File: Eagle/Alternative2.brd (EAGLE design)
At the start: 67 x 53 mm, 19 parts, among them IC2 PCA82C251, Q1 16MHz

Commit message: update1 hw review
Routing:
- net PD0: track 0.00 -> 35.3 mm
- net PB2: track 20.3 -> 0.00 mm, vias 1 -> 0
- net PC5: track 23.4 -> 18.5 mm
- net N$6: track 11.4 -> 15.1 mm, vias 1 -> 0
- net PC4: track 19.0 -> 17.2 mm
- net +5V: track 115.0 -> 116.5 mm
- net N$7: vias 1 -> 0
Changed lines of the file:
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@@
 <contactref element="CT12" pad="1"/>
 <contactref element="U$1" pad="8"/>
-<wire x1="30.1625" y1="8.5725" x2="30.1625" y2="12.065" width="0.4064" layer="1"/>
-<wire x1="30.1625" y1="12.065" x2="29.21" y2="13.0175" width="0.4064" layer="1"/>
-<wire x1="29.21" y1="13.0175" x2="26.6725" y2="13.0175" width="0.4064" layer="1"/>
 <wire x1="39.6875" y1="3.8125" x2="44.935" y2="3.8125" width="0.4064" layer="1"/>
 <wire x1="44.935" y1="3.8125" x2="45.0725" y2="3.95" width="0.4064" layer="1"/>
@@
 <contactref element="U$3" pad="18"/>
 <wire x1="28.0162" y1="8.255" x2="29.845" y2="8.255" width="0.4064" layer="1"/>
-<wire x1="29.845" y1="8.255" x2="30.1625" y2="8.5725" width="0.4064" layer="1"/>
 <wire x1="39.6875" y1="3.8125" x2="34.2875" y2="3.8125" width="0.4064" layer="1"/>
 <wire x1="34.2875" y1="3.8125" x2="29.845" y2="8.255" width="0.4064" layer="1"/>
@@
 <wire x1="19.685" y1="19.05" x2="19.685" y2="21.5425" width="0.4064" layer="1"/>
 <wire x1="19.685" y1="21.5425" x2="19.7325" y2="21.59" width="0.4064" layer="1"/>
-<wire x1="16.825" y1="13.0175" x2="23.81" y2="13.0175" width="0.4064" layer="1"/>
 <wire x1="37.8968" y1="19.3675" x2="39.6875" y2="19.3675" width="0.4064" layer="1"/>
 <wire x1="39.6875" y1="19.3675" x2="40.3225" y2="18.7325" width="0.4064" layer="1"/>
 <wire x1="40.3225" y1="18.7325" x2="40.3225" y2="14.335" width="0.4064" layer="1"/>
-<wire x1="40.3225" y1="14.335" x2="27.035" y2="14.335" width="0.4064" layer="1"/>
-<wire x1="27.035" y1="14.335" x2="26.67" y2="13.97" width="0.4064" layer="1"/>
-<wire x1="26.6725" y1="13.0175" x2="26.67" y2="13.97" width="0" layer="19" extent="1-1"/>
-<wire x1="23.81" y1="13.0175" x2="26.6725" y2="13.0175" width="0" layer="19" extent="1-1"/>
+<wire x1="40.3225" y1="14.335" x2="35.925" y2="14.335" width="0.4064" layer="1"/>
+<wire x1="35.925" y1="14.335" x2="34.6075" y2="13.0175" width="0.4064" layer="1"/>
+<wire x1="34.6075" y1="13.0175" x2="29.845" y2="8.255" width="0.4064" layer="1"/>
+<wire x1="17.4625" y1="13.0175" x2="34.6075" y2="13.0175" width="0.4064" layer="1"/>
+<wire x1="16.825" y1="13.0175" x2="17.4625" y2="13.0175" width="0" layer="19" extent="1-1"/>
 </signal>
 <signal name="PB3">
@@
 <contactref element="SV2" pad="4"/>
 <contactref element="U$1" pad="1"/>
-<wire x1="22.7838" y1="8.255" x2="22.7838" y2="10.0863" width="0.4064" layer="1"/>
-<wire x1="22.7838" y1="8.255" x2="12.065" y2="8.255" width="0.4064" layer="1"/>
-<wire x1="12.065" y1="8.255" x2="10.795" y2="9.525" width="0.4064" layer="1"/>
-<wire x1="10.795" y1="9.525" x2="7.9375" y2="9.525" width="0.4064" layer="1"/>
-<wire x1="7.9375" y1="9.525" x2="6.6675" y2="8.255" width="0.4064" layer="1"/>
+<wire x1="22.7838" y1="8.255" x2="11.1125" y2="8.255" width="0.4064" layer="1"/>
+<wire x1="11.1125" y1="8.255" x2="9.8425" y2="6.985" width="0.4064" layer="1"/>
+<wire x1="9.8425" y1="6.985" x2="7.9375" y2="6.985" width="0.4064" layer="1"/>
+<wire x1="7.9375" y1="6.985" x2="6.6675" y2="8.255" width="0.4064" layer="1"/>
 </signal>
 <signal name="PC5">
 <contactref element="SV2" pad="2"/>
 <contactref element="U$1" pad="2"/>
-<wire x1="6.6675" y1="5.715" x2="7.9375" y2="6.985" width="0.4064" layer="1"/>
-<wire x1="7.9375" y1="6.985" x2="22.7838" y2="6.985" width="0.4064" layer="1"/>
-<wire x1="26.67" y1="11.1125" x2="25.0825" y2="9.525" width="0.4064" layer="1"/>
-<wire x1="25.0825" y1="9.525" x2="25.0825" y2="7.62" width="0.4064" layer="1"/>
-<wire x1="25.0825" y1="7.62" x2="24.4475" y2="6.985" width="0.4064" layer="1"/>
-<wire x1="24.4475" y1="6.985" x2="22.7838" y2="6.985" width="0.4064" layer="1"/>
+<wire x1="22.7838" y1="6.985" x2="13.0175" y2="6.985" width="0.4064" layer="1"/>
+<wire x1="13.0175" y1="6.985" x2="9.525" y2="3.4925" width="0.4064" layer="1"/>
+<wire x1="9.525" y1="3.4925" x2="8.89" y2="3.4925" width="0.4064" layer="1"/>
+<wire x1="8.89" y1="3.4925" x2="6.6675" y2="5.715" width="0.4064" layer="1"/>
 </signal>
 <signal name="N$4">
@@
 <contactref element="IC2" pad="4"/>
 <contactref element="U$3" pad="2"/>
-<wire x1="37.8968" y1="18.0975" x2="35.56" y2="18.0975" width="0.4064" layer="1"/>
-<via x="35.56" y="18.0975" extent="1-16" drill="0.6" shape="square"/>
-<wire x1="35.56" y1="18.0975" x2="35.56" y2="22.86" width="0.4064" layer="16"/>
-<wire x1="35.56" y1="22.86" x2="34.29" y2="24.13" width="0.4064" layer="16"/>
-<wire x1="34.29" y1="24.13" x2="31.75" y2="24.13" width="0.4064" layer="16"/>
+<wire x1="37.8968" y1="18.0975" x2="31.4325" y2="18.0975" width="0.4064" layer="1"/>
+<wire x1="31.4325" y1="18.0975" x2="29.5275" y2="20.0025" width="0.4064" layer="1"/>
+<wire x1="29.5275" y1="20.0025" x2="29.5275" y2="23.495" width="0.4064" layer="1"/>
+<wire x1="29.5275" y1="23.495" x2="30.1625" y2="24.13" width="0.4064" layer="1"/>
+<wire x1="30.1625" y1="24.13" x2="31.75" y2="24.13" width="0.4064" layer="1"/>
 </signal>
 <signal name="N$7">
 <contactref element="IC2" pad="1"/>
 <contactref element="U$3" pad="1"/>
-<wire x1="37.8968" y1="21.9075" x2="34.29" y2="21.9075" width="0.4064" layer="1"/>
-<via x="34.29" y="21.9075" extent="1-16" drill="0.6" shape="square"/>
-<wire x1="34.29" y1="21.9075" x2="32.0675" y2="21.9075" width="0.4064" layer="16"/>
-<wire x1="32.0675" y1="21.9075" x2="31.75" y2="21.59" width="0.4064" layer="16"/>
+<wire x1="37.8968" y1="21.9075" x2="35.2425" y2="21.9075" width="0.4064" layer="1"/>
+<wire x1="35.2425" y1="21.9075" x2="34.925" y2="21.59" width="0.4064" layer="1"/>
+<wire x1="34.925" y1="21.59" x2="31.75" y2="21.59" width="0.4064" layer="1"/>
 </signal>
 <signal name="N$8">
@@
 <contactref element="SV2" pad="3"/>
 <contactref element="U$3" pad="16"/>
-<wire x1="9.2075" y1="8.255" x2="24.13" y2="26.67" width="0" layer="19" extent="1-1"/>
+<wire x1="24.13" y1="26.67" x2="12.3825" y2="26.67" width="0.4064" layer="1"/>
+<wire x1="12.3825" y1="26.67" x2="10.4775" y2="24.765" width="0.4064" layer="1"/>
+<wire x1="10.4775" y1="24.765" x2="8.5725" y2="24.765" width="0.4064" layer="1"/>
+<wire x1="8.5725" y1="24.765" x2="7.9375" y2="24.13" width="0.4064" layer="1"/>
+<wire x1="7.9375" y1="24.13" x2="7.9375" y2="18.0975" width="0.4064" layer="1"/>
+<wire x1="7.9375" y1="18.0975" x2="8.89" y2="17.145" width="0.4064" layer="1"/>
+<wire x1="8.89" y1="17.145" x2="9.8425" y2="17.145" width="0.4064" layer="1"/>
+<wire x1="9.8425" y1="17.145" x2="10.4775" y2="16.51" width="0.4064" layer="1"/>
+<wire x1="10.4775" y1="16.51" x2="10.4775" y2="9.525" width="0.4064" layer="1"/>
+<wire x1="10.4775" y1="9.525" x2="9.2075" y2="8.255" width="0.4064" layer="1"/>
 </signal>
 <signal name="PD1">
@@
 <signal name="PB2">
 <contactref element="SV2" pad="26"/>
-<wire x1="6.6675" y1="36.195" x2="7.9375" y2="37.465" width="0.4064" layer="1"/>
-<wire x1="7.9375" y1="37.465" x2="14.605" y2="37.465" width="0.4064" layer="1"/>
-<via x="14.605" y="37.465" extent="1-16" drill="0.6" shape="square"/>
-<wire x1="14.605" y1="37.465" x2="14.605" y2="29.21" width="0.4064" layer="16"/>
-<wire x1="14.605" y1="29.21" x2="17.145" y2="26.67" width="0.4064" layer="16"/>
 </signal>
 <signal name="N$16">

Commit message: Update2
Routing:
- net +5V: vias 1 -> 0
- net N$4: vias 1 -> 0
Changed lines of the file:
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@@
 <wire x1="27.94" y1="36.83" x2="26.67" y2="38.1" width="0.4064" layer="16"/>
 <wire x1="26.67" y1="38.1" x2="19.3675" y2="38.1" width="0.4064" layer="16"/>
-<wire x1="24.13" y1="21.59" x2="21.9075" y2="21.59" width="0.4064" layer="16"/>
-<via x="21.9075" y="21.59" extent="1-16" drill="0.6" shape="square"/>
-<wire x1="21.9075" y1="21.59" x2="19.7325" y2="21.59" width="0.4064" layer="1"/>
 <wire x1="16.825" y1="13.0175" x2="16.825" y2="16.19" width="0.4064" layer="1"/>
 <wire x1="16.825" y1="16.19" x2="19.685" y2="19.05" width="0.4064" layer="1"/>
@@
 <wire x1="34.6075" y1="13.0175" x2="29.845" y2="8.255" width="0.4064" layer="1"/>
 <wire x1="17.4625" y1="13.0175" x2="34.6075" y2="13.0175" width="0.4064" layer="1"/>
+<wire x1="19.7325" y1="21.59" x2="24.13" y2="21.59" width="0.4064" layer="1"/>
 <wire x1="16.825" y1="13.0175" x2="17.4625" y2="13.0175" width="0" layer="19" extent="1-1"/>
 </signal>
@@
 <wire x1="19.685" y1="25.0825" x2="19.685" y2="24.1775" width="0.4064" layer="1"/>
 <wire x1="19.685" y1="24.1775" x2="19.7325" y2="24.13" width="0.4064" layer="1"/>
-<wire x1="24.13" y1="24.13" x2="21.9075" y2="24.13" width="0.4064" layer="16"/>
-<via x="21.9075" y="24.13" extent="1-16" drill="0.6" shape="square"/>
-<wire x1="21.9075" y1="24.13" x2="19.7325" y2="24.13" width="0.4064" layer="1"/>
+<wire x1="19.7325" y1="24.13" x2="24.13" y2="24.13" width="0.4064" layer="1"/>
 </signal>
 <signal name="N$5">

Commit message: Update3
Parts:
- moved R10 2.54 mm to (47.9, 17.5)
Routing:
- net N$9: track 4.13 -> 6.67 mm
- net PD6: track 23.4 -> 22.4 mm
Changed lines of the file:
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@@
 <attribute name="MF" value="" x="37.1475" y="38.1" size="1.778" layer="27" rot="R90" display="off"/>
 </element>
-<element name="R10" library="rcl" package="R0805" value="120" x="47.9425" y="20.0025" smashed="yes" rot="R270">
-<attribute name="NAME" x="49.2125" y="17.145" size="1.27" layer="25" rot="R3"/>
-<attribute name="VALUE" x="49.2125" y="15.5575" size="1.27" layer="27"/>
+<element name="R10" library="rcl" package="R0805" value="120" x="47.9425" y="17.4625" smashed="yes" rot="R270">
+<attribute name="NAME" x="49.2125" y="14.605" size="1.27" layer="25" rot="R3"/>
+<attribute name="VALUE" x="49.2125" y="13.0175" size="1.27" layer="27"/>
 </element>
 <element name="R8" library="rcl" package="R0805" value="10k" x="15.875" y="13.0175" smashed="yes">
@@
 <wire x1="44.935" y1="3.8125" x2="45.0725" y2="3.95" width="0.4064" layer="1"/>
 <wire x1="9.2075" y1="20.955" x2="10.4775" y2="20.955" width="0.4064" layer="1"/>
-<wire x1="10.4775" y1="20.955" x2="11.43" y2="20.0025" width="0.4064" layer="1"/>
-<wire x1="11.43" y1="20.0025" x2="11.43" y2="12.065" width="0.4064" layer="1"/>
-<wire x1="11.43" y1="12.065" x2="13.0175" y2="10.4775" width="0.4064" layer="1"/>
+<wire x1="10.4775" y1="20.955" x2="12.3825" y2="18.7325" width="0.4064" layer="1"/>
+<wire x1="12.3825" y1="18.7325" x2="12.3825" y2="11.1125" width="0.4064" layer="1"/>
+<wire x1="12.3825" y1="11.1125" x2="13.0175" y2="10.4775" width="0.4064" layer="1"/>
 <wire x1="13.0175" y1="10.4775" x2="16.1925" y2="10.4775" width="0.4064" layer="1"/>
 <wire x1="16.1925" y1="10.4775" x2="16.8275" y2="11.1125" width="0.4064" layer="1"/>
@@
 <wire x1="41.5925" y1="20.0025" x2="41.5925" y2="17.4625" width="0.4064" layer="1"/>
 <wire x1="41.5925" y1="17.4625" x2="42.545" y2="16.51" width="0.4064" layer="1"/>
-<wire x1="42.545" y1="16.51" x2="47.3075" y2="16.51" width="0.4064" layer="1"/>
-<wire x1="47.3075" y1="16.51" x2="47.9425" y2="17.145" width="0.4064" layer="1"/>
-<wire x1="47.9425" y1="17.145" x2="47.9425" y2="19.0525" width="0.4064" layer="1"/>
-<wire x1="47.9425" y1="19.0525" x2="49.85" y2="19.0525" width="0.4064" layer="1"/>
 <via x="50.4825" y="22.86" extent="1-16" drill="0.6" shape="square"/>
 <wire x1="50.4825" y1="22.86" x2="50.4825" y2="23.495" width="0.4064" layer="16"/>
@@
 <wire x1="51.435" y1="24.4475" x2="57.3659" y2="24.4475" width="0.4064" layer="16"/>
 <wire x1="57.3659" y1="24.4475" x2="57.4675" y2="24.5491" width="0.4064" layer="16"/>
-<wire x1="49.85" y1="19.0525" x2="50.4825" y2="19.685" width="0.4064" layer="1"/>
-<wire x1="50.4825" y1="19.685" x2="50.4825" y2="22.86" width="0.4064" layer="1"/>
+<wire x1="50.4825" y1="18.0975" x2="50.4825" y2="22.86" width="0.4064" layer="1"/>
+<wire x1="42.545" y1="16.51" x2="47.94" y2="16.51" width="0.4064" layer="1"/>
+<wire x1="47.94" y1="16.51" x2="47.9425" y2="16.5125" width="0.4064" layer="1"/>
+<wire x1="47.9425" y1="16.5125" x2="48.8975" y2="16.5125" width="0.4064" layer="1"/>
+<wire x1="48.8975" y1="16.5125" x2="50.4825" y2="18.0975" width="0.4064" layer="1"/>
 </signal>
 <signal name="N$9">
 <contactref element="JP1" pad="1"/>
 <contactref element="R10" pad="1"/>
-<wire x1="47.9425" y1="25.0825" x2="47.9425" y2="22.86" width="0.4064" layer="16"/>
-<via x="47.9425" y="22.86" extent="1-16" drill="0.6" shape="square"/>
-<wire x1="47.9425" y1="22.86" x2="47.9425" y2="20.9525" width="0.4064" layer="1"/>
+<wire x1="47.9425" y1="25.0825" x2="47.9425" y2="21.59" width="0.4064" layer="16"/>
+<via x="47.9425" y="21.59" extent="1-16" drill="0.6" shape="square"/>
+<wire x1="47.9425" y1="21.59" x2="47.9425" y2="18.4125" width="0.4064" layer="1"/>
 </signal>
 <signal name="N$10">
@@
 <contactref element="SV2" pad="23"/>
 <contactref element="SV1" pad="2"/>
-<wire x1="9.2075" y1="33.655" x2="16.1925" y2="33.655" width="0.4064" layer="1"/>
-<via x="16.1925" y="33.655" extent="1-16" drill="0.6" shape="square"/>
-<wire x1="16.1925" y1="33.655" x2="16.1925" y2="46.6725" width="0.4064" layer="16"/>
-<wire x1="16.1925" y1="46.6725" x2="16.8275" y2="47.3075" width="0.4064" layer="16"/>
+<wire x1="9.2075" y1="33.655" x2="14.605" y2="33.655" width="0.4064" layer="1"/>
+<via x="14.605" y="33.655" extent="1-16" drill="0.6" shape="square"/>
+<wire x1="14.605" y1="33.655" x2="14.605" y2="44.7675" width="0.4064" layer="16"/>
+<wire x1="14.605" y1="44.7675" x2="16.8275" y2="47.3075" width="0.4064" layer="16"/>
 <wire x1="16.8275" y1="47.3075" x2="19.3675" y2="47.3075" width="0.4064" layer="16"/>
 </signal>

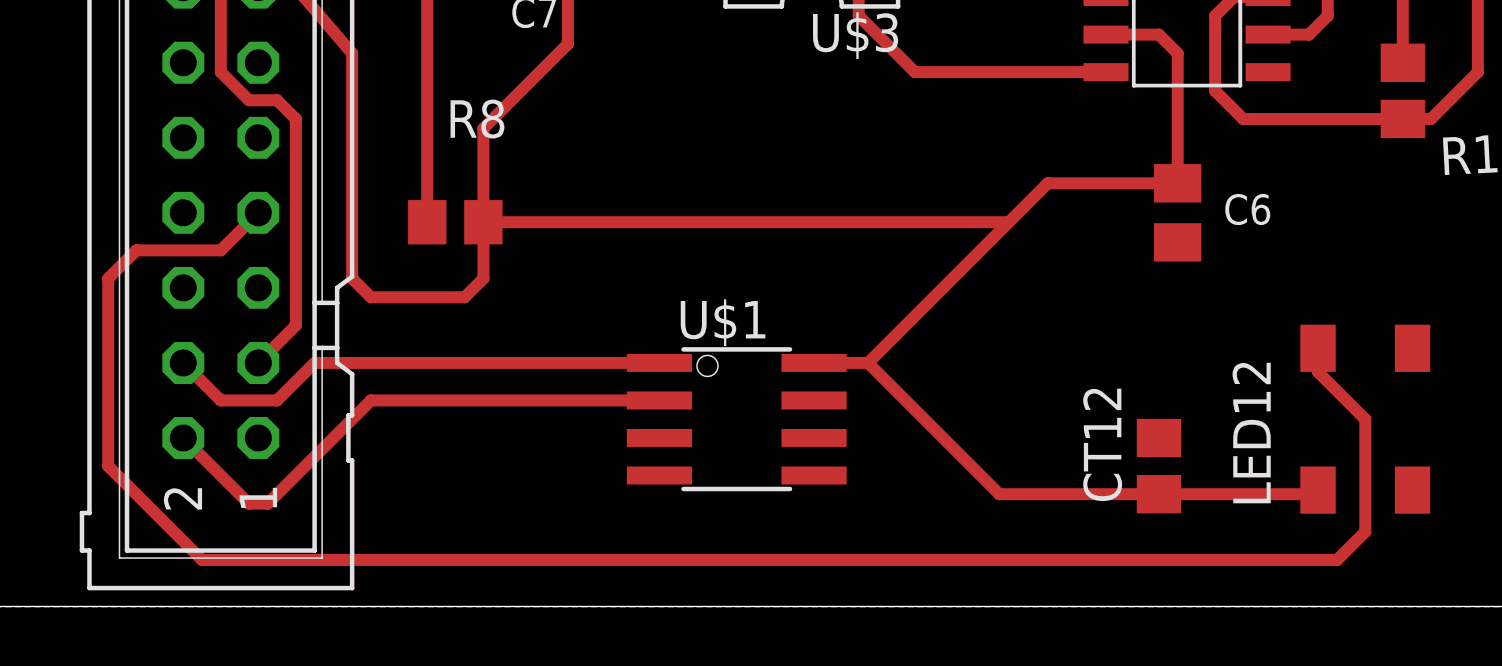
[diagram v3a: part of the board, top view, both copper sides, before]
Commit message: changes in 5V route
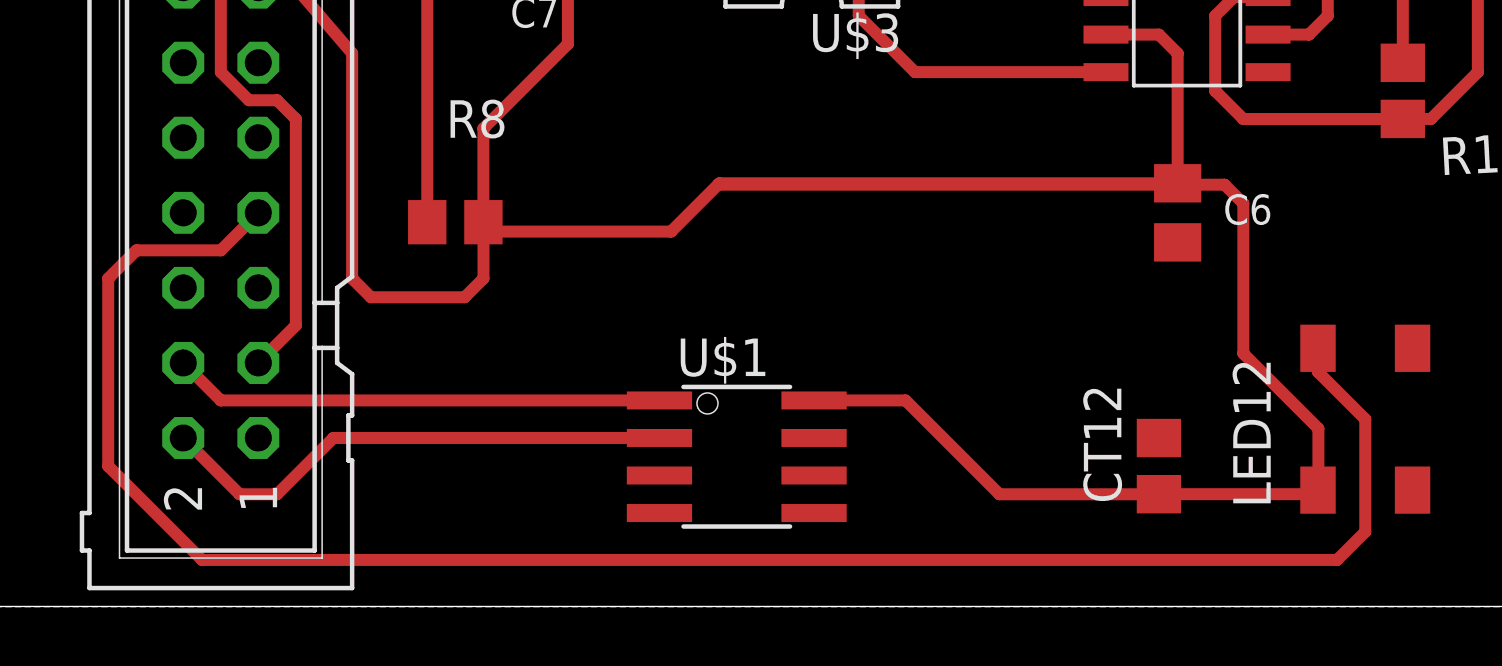
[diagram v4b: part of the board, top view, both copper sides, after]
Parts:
- moved U$1 1.27 mm to (25.4, 5.08)
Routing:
- net +5V: track 116.5 -> 138.9 mm
- net PC5: track 18.5 -> 17.7 mm
- net PC4: track 17.2 -> 16.6 mm
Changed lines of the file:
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@@
 <element name="LED12" library="sp2" package="WS2812_4" value="WS2812_4H" x="46.6725" y="6.35" rot="R90"/>
 <element name="CT12" library="rcl" package="C0805" value="100n" x="39.6875" y="4.7625" rot="R90"/>
-<element name="U$1" library="sp2" package="SO08" value="" x="25.4" y="6.35" rot="R270"/>
+<element name="U$1" library="sp2" package="SO08" value="" x="25.4" y="5.08" rot="R270"/>
 <element name="U$3" library="sp2" package="DIL18" value="MCP2515PDIP" x="27.94" y="31.75" rot="R90"/>
 </elements>
@@
 <wire x1="16.8275" y1="12.6975" x2="16.825" y2="13.0175" width="0.4064" layer="1"/>
 <contactref element="U$3" pad="18"/>
-<wire x1="28.0162" y1="8.255" x2="29.845" y2="8.255" width="0.4064" layer="1"/>
-<wire x1="39.6875" y1="3.8125" x2="34.2875" y2="3.8125" width="0.4064" layer="1"/>
-<wire x1="34.2875" y1="3.8125" x2="29.845" y2="8.255" width="0.4064" layer="1"/>
 <wire x1="24.13" y1="21.59" x2="26.67" y2="21.59" width="0.4064" layer="16"/>
 <wire x1="26.67" y1="21.59" x2="27.94" y2="22.86" width="0.4064" layer="16"/>
@@
 <wire x1="39.6875" y1="19.3675" x2="40.3225" y2="18.7325" width="0.4064" layer="1"/>
 <wire x1="40.3225" y1="18.7325" x2="40.3225" y2="14.335" width="0.4064" layer="1"/>
-<wire x1="40.3225" y1="14.335" x2="35.925" y2="14.335" width="0.4064" layer="1"/>
-<wire x1="35.925" y1="14.335" x2="34.6075" y2="13.0175" width="0.4064" layer="1"/>
-<wire x1="34.6075" y1="13.0175" x2="29.845" y2="8.255" width="0.4064" layer="1"/>
-<wire x1="17.4625" y1="13.0175" x2="34.6075" y2="13.0175" width="0.4064" layer="1"/>
 <wire x1="19.7325" y1="21.59" x2="24.13" y2="21.59" width="0.4064" layer="1"/>
-<wire x1="16.825" y1="13.0175" x2="17.4625" y2="13.0175" width="0" layer="19" extent="1-1"/>
+<wire x1="28.0162" y1="6.985" x2="31.115" y2="6.985" width="0.4064" layer="1"/>
+<wire x1="31.115" y1="6.985" x2="34.29" y2="3.81" width="0.4064" layer="1"/>
+<wire x1="34.29" y1="3.81" x2="39.685" y2="3.81" width="0.4064" layer="1"/>
+<wire x1="39.685" y1="3.81" x2="39.6875" y2="3.8125" width="0.4064" layer="1"/>
+<wire x1="40.3225" y1="14.335" x2="24.8125" y2="14.335" width="0.4064" layer="1"/>
+<wire x1="24.8125" y1="14.335" x2="24.765" y2="14.2875" width="0.4064" layer="1"/>
+<wire x1="23.1775" y1="12.7" x2="17.1425" y2="12.7" width="0.4064" layer="1"/>
+<wire x1="17.1425" y1="12.7" x2="16.825" y2="13.0175" width="0.4064" layer="1"/>
+<wire x1="23.1775" y1="12.7" x2="24.765" y2="14.2875" width="0.4064" layer="1"/>
+<wire x1="24.765" y1="14.2875" x2="41.91" y2="14.2875" width="0.4064" layer="1"/>
+<wire x1="41.91" y1="14.2875" x2="42.545" y2="13.6525" width="0.4064" layer="1"/>
+<wire x1="42.545" y1="13.6525" x2="42.545" y2="8.5725" width="0.4064" layer="1"/>
+<wire x1="42.545" y1="8.5725" x2="45.085" y2="6.0325" width="0.4064" layer="1"/>
+<wire x1="45.085" y1="6.0325" x2="45.085" y2="3.9625" width="0.4064" layer="1"/>
+<wire x1="45.085" y1="3.9625" x2="45.0725" y2="3.95" width="0.4064" layer="1"/>
 </signal>
 <signal name="PB3">
@@
 <contactref element="SV2" pad="4"/>
 <contactref element="U$1" pad="1"/>
-<wire x1="22.7838" y1="8.255" x2="11.1125" y2="8.255" width="0.4064" layer="1"/>
-<wire x1="11.1125" y1="8.255" x2="9.8425" y2="6.985" width="0.4064" layer="1"/>
-<wire x1="9.8425" y1="6.985" x2="7.9375" y2="6.985" width="0.4064" layer="1"/>
+<wire x1="22.7838" y1="6.985" x2="7.9375" y2="6.985" width="0.4064" layer="1"/>
 <wire x1="7.9375" y1="6.985" x2="6.6675" y2="8.255" width="0.4064" layer="1"/>
 </signal>
@@
 <contactref element="SV2" pad="2"/>
 <contactref element="U$1" pad="2"/>
-<wire x1="22.7838" y1="6.985" x2="13.0175" y2="6.985" width="0.4064" layer="1"/>
-<wire x1="13.0175" y1="6.985" x2="9.525" y2="3.4925" width="0.4064" layer="1"/>
-<wire x1="9.525" y1="3.4925" x2="8.89" y2="3.4925" width="0.4064" layer="1"/>
-<wire x1="8.89" y1="3.4925" x2="6.6675" y2="5.715" width="0.4064" layer="1"/>
+<wire x1="22.7838" y1="5.715" x2="11.7475" y2="5.715" width="0.4064" layer="1"/>
+<wire x1="11.7475" y1="5.715" x2="9.8425" y2="3.81" width="0.4064" layer="1"/>
+<wire x1="9.8425" y1="3.81" x2="8.5725" y2="3.81" width="0.4064" layer="1"/>
+<wire x1="8.5725" y1="3.81" x2="6.6675" y2="5.715" width="0.4064" layer="1"/>
 </signal>
 <signal name="N$4">
